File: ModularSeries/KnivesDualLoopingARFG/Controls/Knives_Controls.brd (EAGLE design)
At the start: 48.5 x 100 mm, 17 parts, among them SW1 SPDT_SWITCHDW1, SW2 SPDT_SWITCHDW1

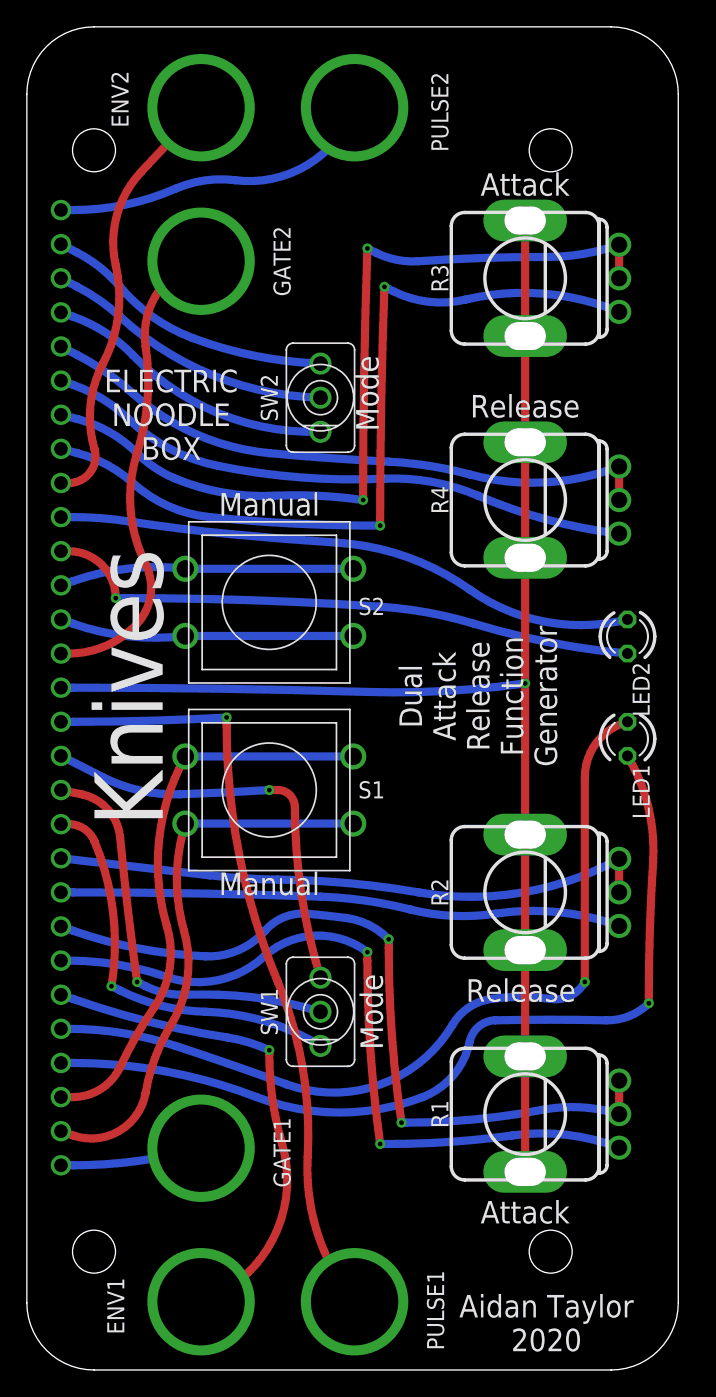
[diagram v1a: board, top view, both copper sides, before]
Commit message: Updates to Portals and Knives, Panel layout for Prism and Knives added
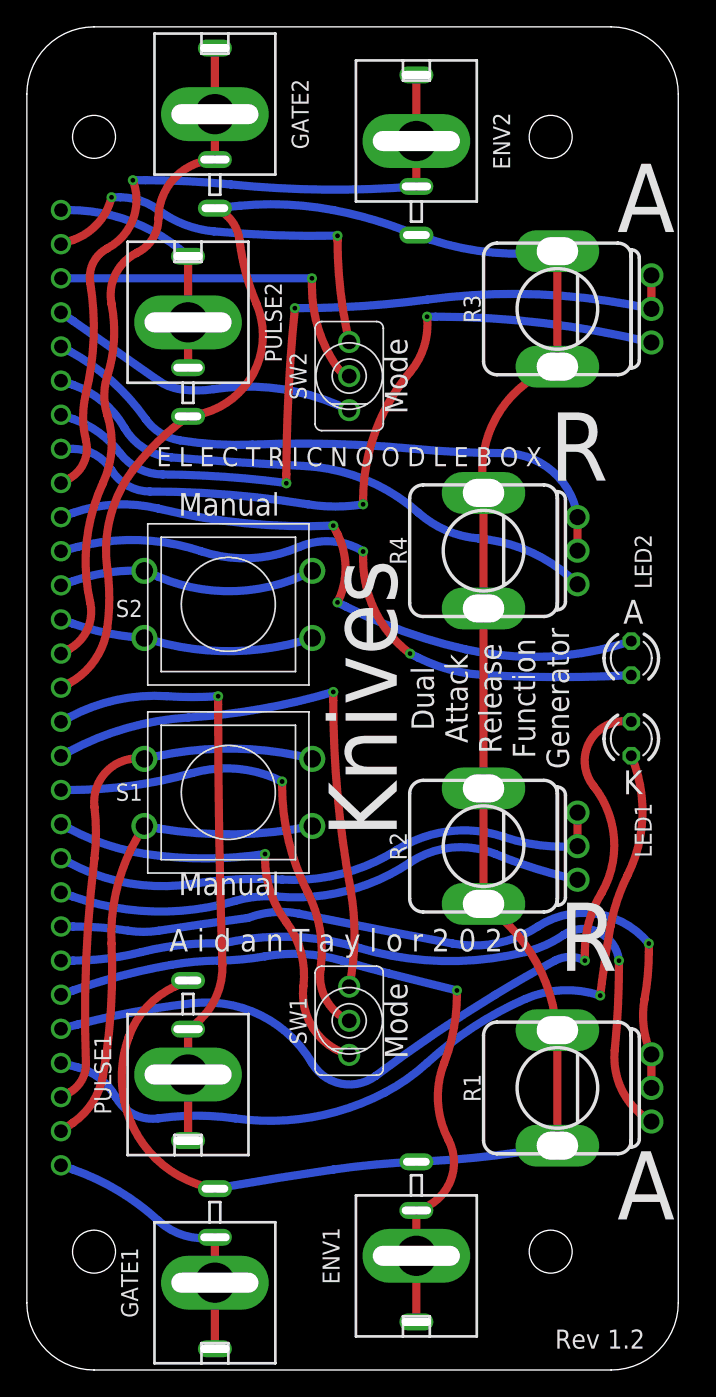
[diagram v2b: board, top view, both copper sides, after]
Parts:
- ENV1, ENV2, GATE1, GATE2, PULSE1, PULSE2: value BANANA_PANEL -> COMBI-JACKCINCHNANA; device ElectricNoodleBox:BANANA_PANEL -> ElectricNoodleBox:NEWCOMBOJACK_PANEL
- moved PULSE1 21.0 mm to (13.0, 22.0), turned to 180 degrees
- moved PULSE2 20.2 mm to (13.0, 78.0)
- moved ENV1 16.4 mm to (30.0, 8.50), turned to 180 degrees
- moved ENV2 16.2 mm to (30.0, 91.5)
- moved GATE2 11.0 mm to (15.0, 93.5)
- moved GATE1 10.1 mm to (15.0, 6.50), turned to 180 degrees
- moved R4 4.88 mm to (35.0, 61.0)
- moved R2 4.63 mm to (35.0, 39.0)
- moved R3 3.31 mm to (40.5, 79.0)
- moved R1 3.09 mm to (40.5, 21.0)
- moved S1 3.06 mm to (16.0, 43.0)
- moved S2 3.05 mm to (16.0, 57.0)
- moved SW2 2.68 mm to (25.0, 74.0)
- moved SW1 2.24 mm to (25.0, 26.0)
- moved LED2 1.63 mm to (46.0, 53.0)
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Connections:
- removed net N$29: BOARD1.GND, R1.LUGL, R1.LUGR, R2.LUGL, R2.LUGR, R3.LUGL, R3.LUGR, R4.LUGL, R4.LUGR
- new net AGND: BOARD1.GND, ENV1.S, ENV2.S, GATE1.S, GATE2.S, PULSE1.S, PULSE2.S, R1.LUGL, R1.LUGR, R2.LUGL, R2.LUGR, R3.LUGL, R3.LUGR, R4.LUGL, R4.LUGR
- net N$1: now also GATE1.T1, GATE1.T2
- net N$14: now also PULSE1.T1, PULSE1.T2
- net N$15: now also GATE2.T1, GATE2.T2
- net N$20: now also ENV2.T1, ENV2.T2
- net N$28: now also PULSE2.T1, PULSE2.T2
- net N$6: now also ENV1.T1, ENV1.T2
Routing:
- net AGND: track 0.00 -> 183.2 mm
- net N$29: track 105.4 -> 0.00 mm, vias 1 -> 0
- net N$20: track 31.3 -> 53.2 mm, vias 0 -> 1
- net N$6: track 36.3 -> 55.4 mm
- net N$15: track 34.4 -> 48.4 mm
- net N$13: track 31.3 -> 42.9 mm
- net N$14: track 57.0 -> 45.7 mm
- net N$1: track 10.5 -> 21.0 mm
- net N$27: track 21.8 -> 30.5 mm, vias 0 -> 2
- net N$18: track 43.1 -> 48.7 mm, vias 0 -> 2
- net N$22: track 60.3 -> 55.0 mm
- net N$26: track 21.3 -> 26.7 mm, vias 0 -> 1
- net N$28: track 23.6 -> 18.4 mm
- net N$12: track 30.6 -> 35.3 mm
- net N$21: track 64.1 -> 60.2 mm
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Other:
- board text added: "A"
- board text added: "A i d a n T a y l o r 2 0 2 0"
- board text added: "E L E C T R I C N O O D L E B O X"
- board text added: "K"
- board text added: "R"
- board text added: "Rev 1.2"
- board text removed: "Aidan Taylor 2020"
- board text removed: "Attack"
- board text removed: "ELECTRIC NOODLE BOX"
- board text removed: "Release"

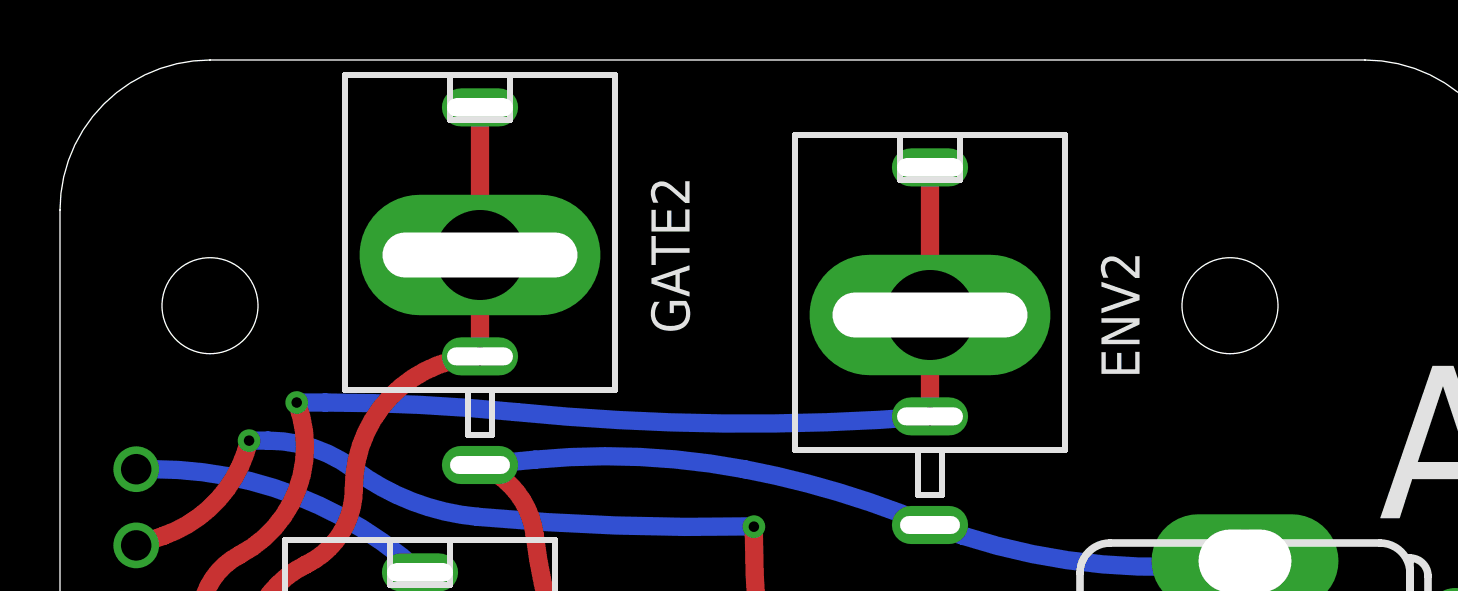
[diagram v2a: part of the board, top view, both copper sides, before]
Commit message: Pulse output fixed on Knives, schematics and layout updated. Panel added for Portals
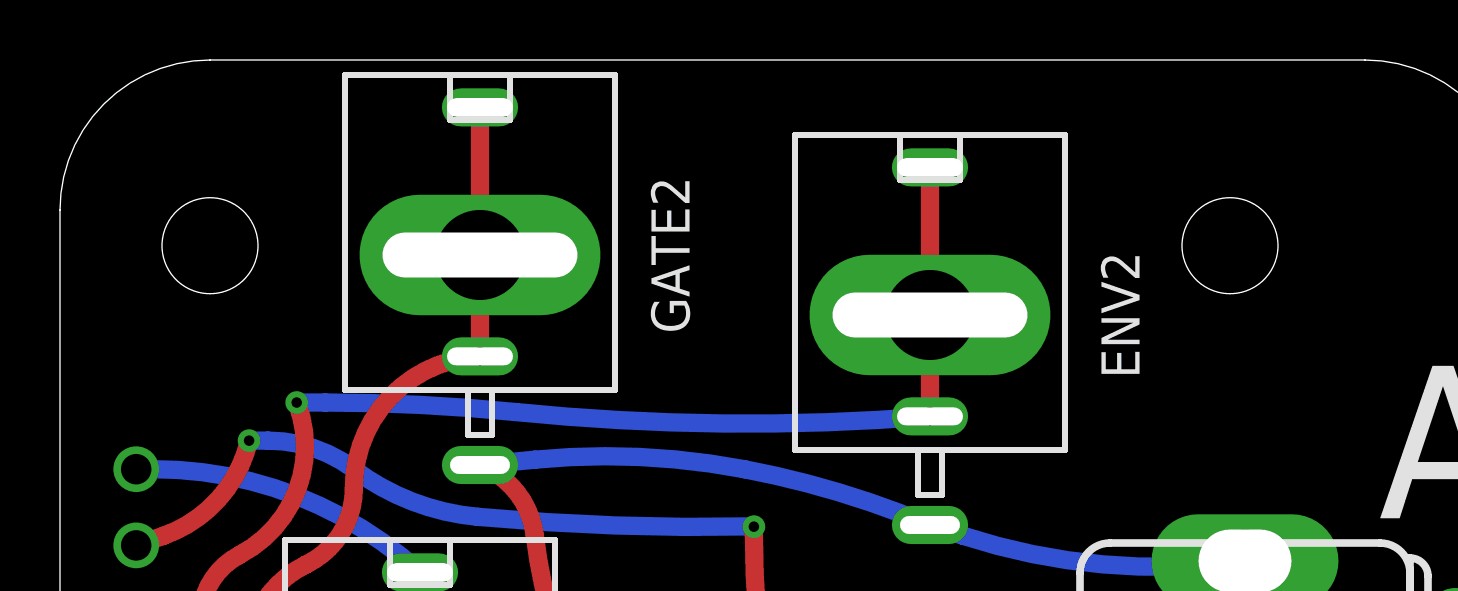
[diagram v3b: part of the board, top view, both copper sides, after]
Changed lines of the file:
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@@
 <mfgpreviewcolor name="substratecolor" color="0xFF786E46"/>
 </mfgpreviewcolors>
+<errors>
+</errors>
 </board>
 </drawing>

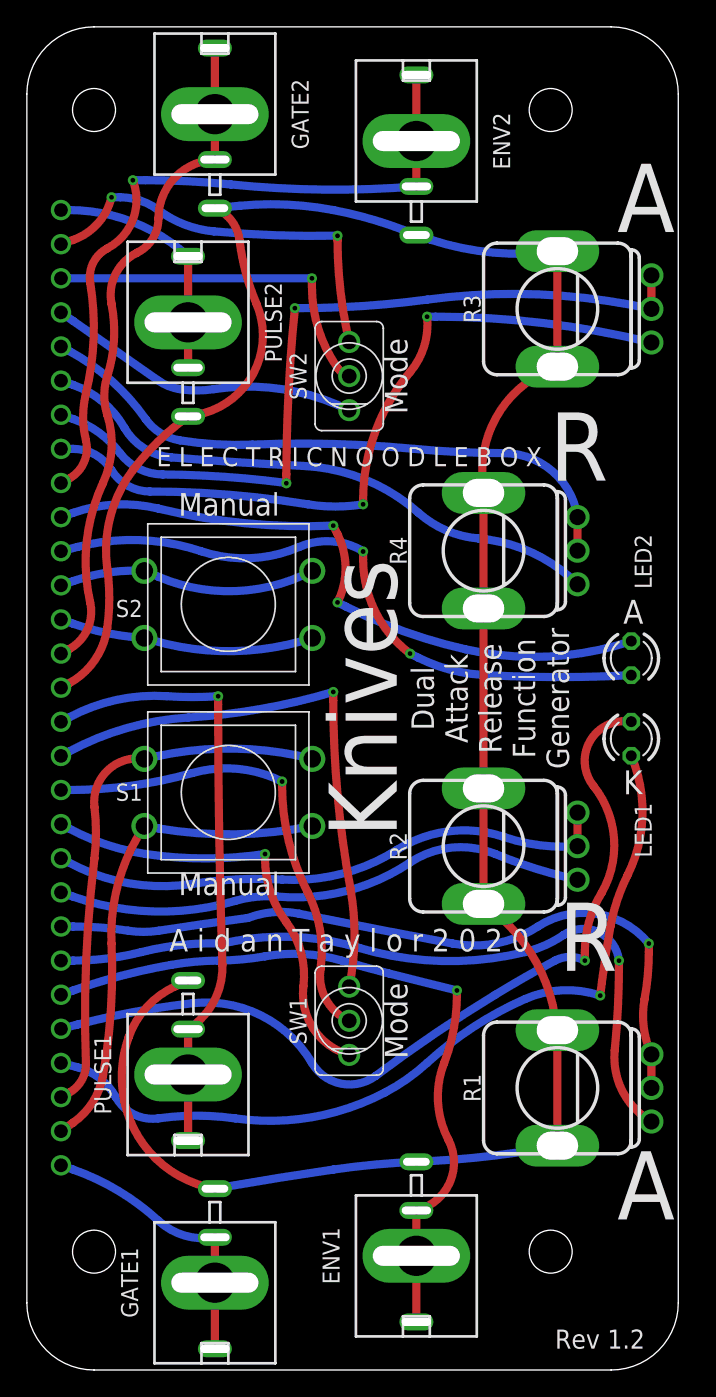
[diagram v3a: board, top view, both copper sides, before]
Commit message: Panel for TimeSeeds added. TLHP core PCB added
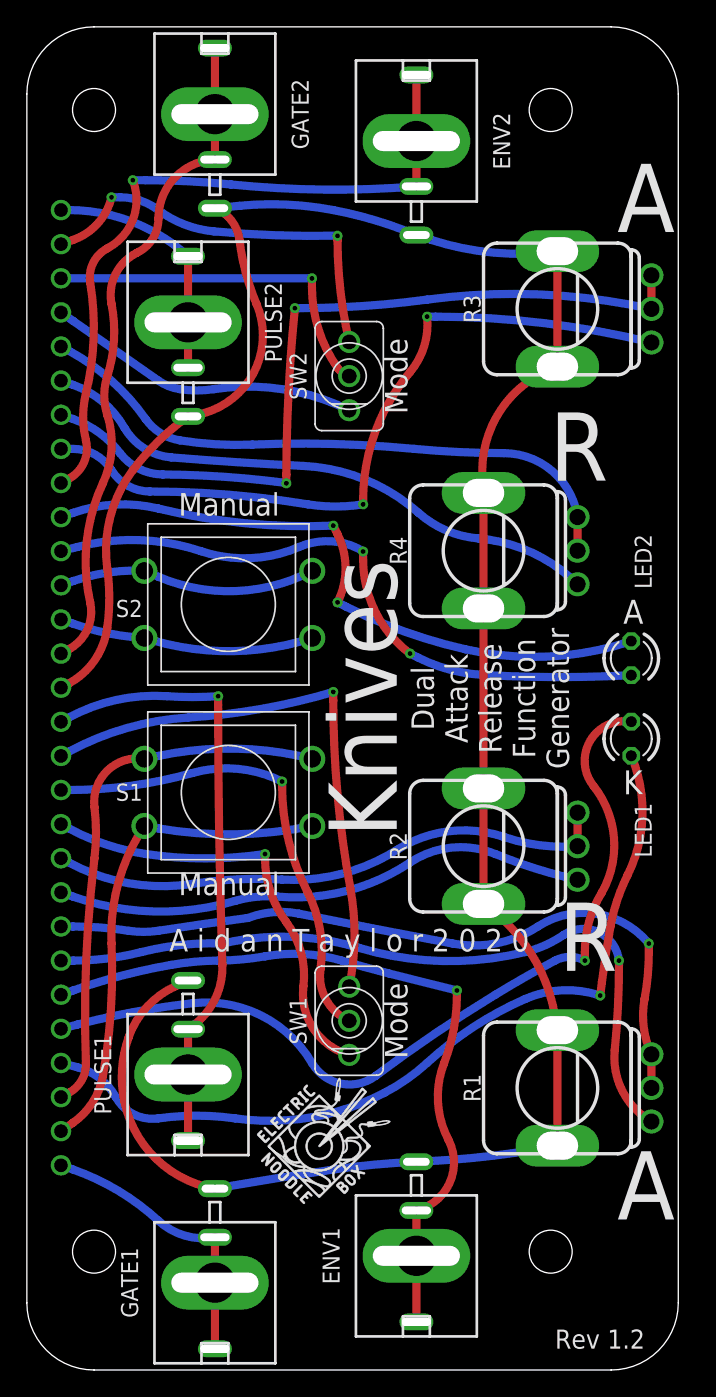
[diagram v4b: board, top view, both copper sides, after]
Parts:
- added U$1, U$2: (no value), ElectricNoodleBox:LOGO10X10
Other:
- board text removed: "E L E C T R I C N O O D L E B O X"
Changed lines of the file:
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@@
 <text x="28.5" y="26" size="1.6764" layer="21" font="vector" ratio="16" rot="R90" align="center">Mode</text>
 <text x="28.5" y="74" size="1.6764" layer="21" font="vector" ratio="16" rot="R90" align="center">Mode</text>
-<text x="25" y="68" size="1.4224" layer="21" font="vector" ratio="16" align="center">E L E C T R I C N O O D L E B O X</text>
 <text x="25" y="32" size="1.6764" layer="21" font="vector" ratio="16" align="center">A i d a n T a y l o r 2 0 2 0</text>
 <text x="45.4025" y="55.5625" size="1.778" layer="21">A</text>
@@
 <attribute name="NAME" x="19.35" y="78" size="1.27" layer="25" font="vector" rot="R90" align="center"/>
 </element>
+<element name="U$1" library="ElectricNoodleBox" package="LOGO10X10" value="" x="18.0975" y="12.065" smashed="yes"/>
+<element name="U$2" library="ElectricNoodleBox" package="LOGO10X10" value="" x="27.94" y="12.3825" smashed="yes" rot="MR0"/>
 </elements>
 <signals>

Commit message: Layout and schematic renders for LHP added
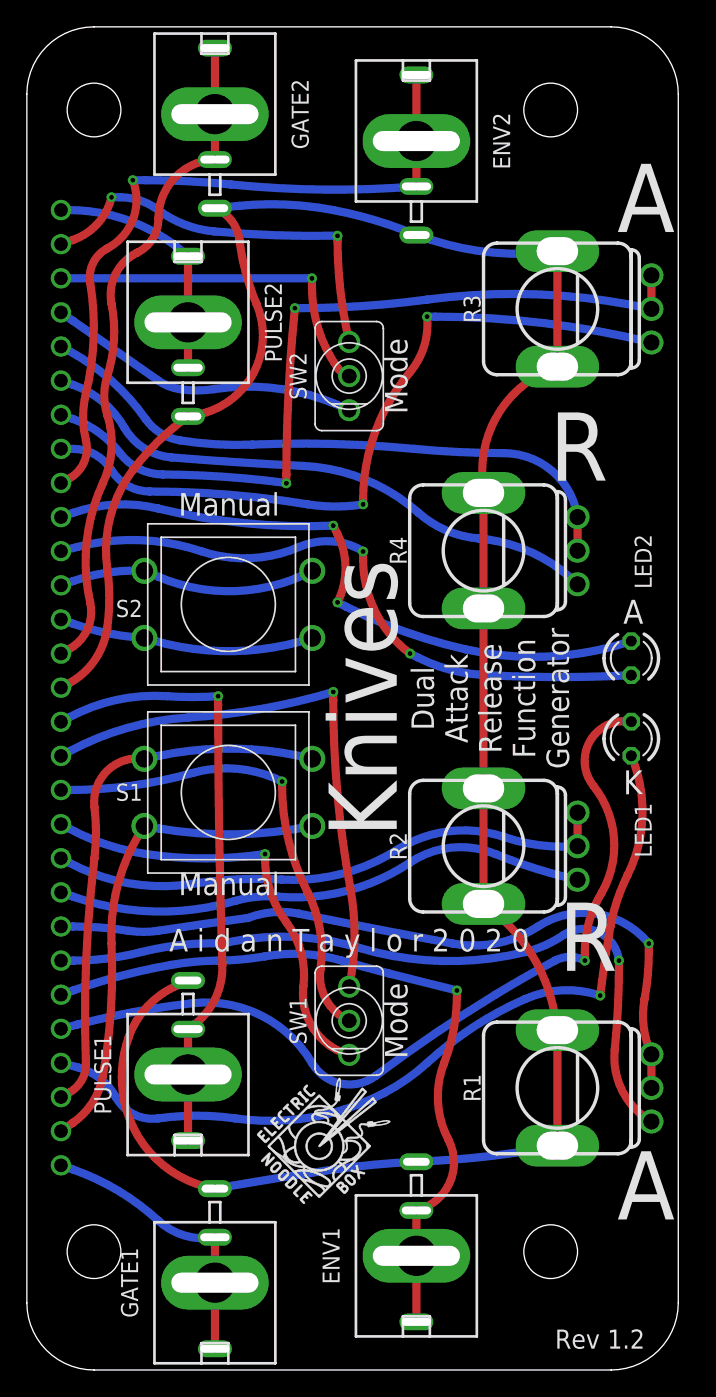
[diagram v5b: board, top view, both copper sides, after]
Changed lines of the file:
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@@
 <?xml version="1.0" encoding="utf-8"?>
 <!DOCTYPE eagle SYSTEM "eagle.dtd">
-<eagle version="9.6.0">
+<eagle version="9.6.2">
 <drawing>
 <settings>
@@
 </layers>
 <board>
-<fusionsync huburn="a.cGVyc29uYWw6dWUyYjdlNGE0" projecturn="a.cGVyc29uYWw6dWUyYjdlNGE0IzIwMjAwNDA1MjgzMzA0MTgx" f3durn="urn:adsk.wipprod:dm.lineage:oC09-YXSQA24y2Jj-FFeLQ" pcbguid="ee4c84e1-cc95-4fbf-8034-87506709d442" lastpulledtime="" lastsyncedchangeguid="" latestrevisionid="9adcb5d0-0b36-4c77-bb2c-7c3273a816b2" lastsyncedrevisionid="9adcb5d0-0b36-4c77-bb2c-7c3273a816b2" lastboardhashguid="28fda7e2-0331-2b42-54da-74230740688f" lastpushedtime="2020-05-28T10:07:59Z" linktopcb3d="%12"/>
+<fusionsync huburn="a.cGVyc29uYWw6dWUyYjdlNGE0" projecturn="a.cGVyc29uYWw6dWUyYjdlNGE0IzIwMjAwNDA1MjgzMzA0MTgx" f3durn="urn:adsk.wipprod:dm.lineage:oC09-YXSQA24y2Jj-FFeLQ" pcbguid="ee4c84e1-cc95-4fbf-8034-87506709d442" lastpulledtime="" lastsyncedchangeguid="" latestrevisionid="9adcb5d0-0b36-4c77-bb2c-7c3273a816b2" lastsyncedrevisionid="9adcb5d0-0b36-4c77-bb2c-7c3273a816b2" lastboardhashguid="28fda7e2-0331-2b42-54da-74230740688f" lastpushedtime="2020-05-28T10:07:59Z" linktopcb3d="true"/>
 <plain>
 <wire x1="49.5" y1="5" x2="49.5" y2="95" width="0" layer="20"/>
